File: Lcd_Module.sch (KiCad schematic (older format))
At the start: 1 part

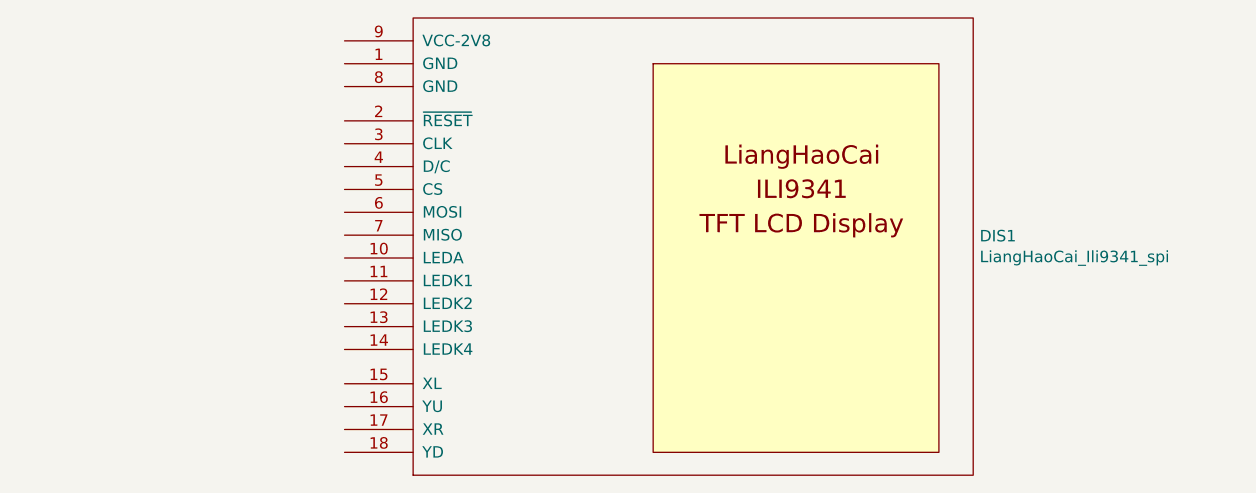
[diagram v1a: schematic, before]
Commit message: Added logic level shifter on pcb
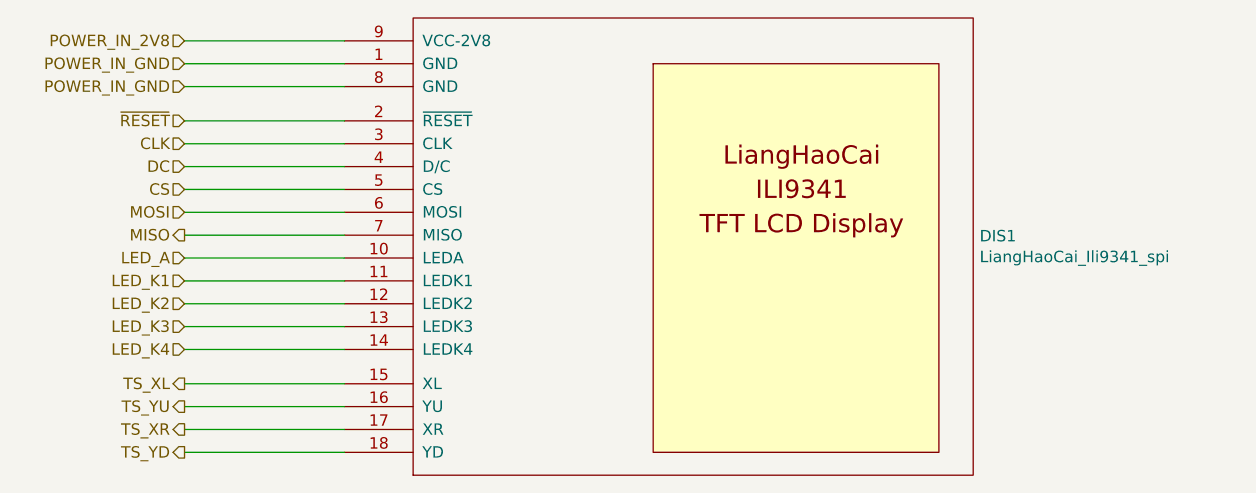
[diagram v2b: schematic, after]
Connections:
- net POWER_IN_GND: now reaches DIS1.1 (GND)
- net POWER_IN_GND: now also DIS1.8 (GND)
- net LED_A: now reaches DIS1.10 (LEDA)
- net LED_K1: now reaches DIS1.11 (LEDK1)
- net LED_K2: now reaches DIS1.12 (LEDK2)
- net LED_K3: now reaches DIS1.13 (LEDK3)
- net LED_K4: now reaches DIS1.14 (LEDK4)
- net TS_XL: now reaches DIS1.15 (XL)
- net TS_YU: now reaches DIS1.16 (YU)
- net TS_XR: now reaches DIS1.17 (XR)
- net TS_YD: now reaches DIS1.18 (YD)
- net ~RESET: now reaches DIS1.2 (~RESET)
- net CLK: now reaches DIS1.3 (CLK)
- net DC: now reaches DIS1.4 (D/C)
- net CS: now reaches DIS1.5 (CS)
- net MOSI: now reaches DIS1.6 (MOSI)
- net MISO: now reaches DIS1.7 (MISO)
- net POWER_IN_2V8: now reaches DIS1.9 (VCC-2V8)
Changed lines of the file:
@@
 $Descr A3 16535 11693
 encoding utf-8
-Sheet 3 6
+Sheet 3 8
 Title "LCD Module"
 Date "2020-11-14"
@@
 	1    0    0    -1
 $EndComp
+Text HLabel 5950 4400 0    50   Input ~ 0
+POWER_IN_2V8
+Text HLabel 5950 4500 0    50   Input ~ 0
+POWER_IN_GND
+Text HLabel 5950 4600 0    50   Input ~ 0
+POWER_IN_GND
+Text HLabel 5950 4750 0    50   Input ~ 0
+~RESET
+Text HLabel 5950 4850 0    50   Input ~ 0
+CLK
+Text HLabel 5950 4950 0    50   Input ~ 0
+DC
+Text HLabel 5950 5050 0    50   Input ~ 0
+CS
+Text HLabel 5950 5150 0    50   Input ~ 0
+MOSI
+Text HLabel 5950 5250 0    50   Output ~ 0
+MISO
+Text HLabel 5950 5350 0    50   Input ~ 0
+LED_A
+Text HLabel 5950 5450 0    50   Input ~ 0
+LED_K1
+Text HLabel 5950 5550 0    50   Input ~ 0
+LED_K2
+Text HLabel 5950 5650 0    50   Input ~ 0
+LED_K3
+Text HLabel 5950 5750 0    50   Input ~ 0
+LED_K4
+Text HLabel 5950 5900 0    50   Output ~ 0
+TS_XL
+Text HLabel 5950 6000 0    50   Output ~ 0
+TS_YU
+Text HLabel 5950 6100 0    50   Output ~ 0
+TS_XR
+Text HLabel 5950 6200 0    50   Output ~ 0
+TS_YD
+Wire Wire Line
+	6650 4400 5950 4400
+Wire Wire Line
+	5950 4500 6650 4500
+Wire Wire Line
+	6650 4600 5950 4600
+Wire Wire Line
+	6650 4750 5950 4750
+Wire Wire Line
+	5950 4850 6650 4850
+Wire Wire Line
+	6650 4950 5950 4950
+Wire Wire Line
+	6650 5050 5950 5050
+Wire Wire Line
+	6650 5150 5950 5150
+Wire Wire Line
+	6650 5250 5950 5250
+Wire Wire Line
+	5950 5350 6650 5350
+Wire Wire Line
+	6650 5450 5950 5450
+Wire Wire Line
+	6650 5550 5950 5550
+Wire Wire Line
+	6650 5650 5950 5650
+Wire Wire Line
+	6650 5750 5950 5750
+Wire Wire Line
+	6650 5900 5950 5900
+Wire Wire Line
+	5950 6000 6650 6000
+Wire Wire Line
+	6650 6100 5950 6100
+Wire Wire Line
+	6650 6200 5950 6200
 $EndSCHEMATC
